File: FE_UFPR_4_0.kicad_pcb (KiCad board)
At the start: 4 copper layers, 146 x 130 mm, 369 parts, among them J1 Mini-Fit Jr 5566-02A, J2 DSUB-37_Socket, J20 LaunchPad J1+J3, J21 LaunchPad J4+J2, J22 LaunchPad J5+J7, J23 LaunchPad J8+J6, J3 LEM DTM13-12PA-R005 key A, J4 ENC DTM13-12PB-R005 key B, J5 VEH DTM13-08PA-R004 key A, Q1 SQD50P06-15L, U1 LMR33630ADDAR, U10 SN74LVC2G17DBVR, U11 SN74LVC2G17DBVR, U12 OPA2376, U13 OPA2376, U14 OPA2376, U15 OPA2376, U16 OPA2376, U17 OPA2376, U18 SN65HVD230DR, U19 LTV-817S-TA1-C, U2 TPS62933FDRLR, U20 LTV-817S-TA1-C, U21 SN74LVC2G17DBVR, U3 AMS1117-3.3, U4 URA2415YMD-6WR3, U5 UCC27524DR, U6 UCC27524DR, U7 UCC27524DR, U8 SN74LVC1G11DBVR, U9 SN74LVC2G17DBVR

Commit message: S9.5: motor temperature channel (EMRAX KTY81-210) on J4 cavities 6/7
The board had no motor-temperature channel at all, and the EMRAX manual
makes one mandatory: the sensor "must be connected to the controller",
120 C on the copper windings voids the warranty, and on sensor
disconnection "the controller has to stop the motor". Captured now
because the board is placed but not yet routed.

Circuit: KTY81-210 as the divider's BOTTOM leg, excited from +3V3 through
R129 2.20k 0.1%. Open -> 3.30 V, short -> 0 V, both outside the valid
1.12-2.18 V band, so disconnect detection is free. +3V3 rather than +5V
so an open sensor cannot exceed the ADC's VDDA+0.3 absolute maximum.
6.25 codes/K at the 120 C limit. R131/R132 monitor the excitation rail on
ADCINA3 so firmware cancels it exactly - without that the LDO's +/-2 % is
+/-10 K, larger than the sensor's own +/-4.7 K.

J4 cavities 6/7 with 5/8 left empty as a guard column; ADC = ADCINB3 on
J20 pad 10. Zero new BOM lines - every part reuses an existing LCSC code.

GATED: legal only if EMRAX confirms the KTY is reinforced-insulated from
the windings. Basic insulation makes it a tractive-system conductor
(FSAE 2026 EV.1.6) and EV.6.5.3 forbids it sharing J4 with the encoder.

Also fixes a PRE-EXISTING defect: sync_schematic_to_board lists nets in
nets_added that it never assigns to pads. +5V_VEH and CAN_RS had ZERO pad
assignments on the board, including in the S9 commit - S10 would have
routed with the ECU supply feed and the CAN slope resistor unconnected.
All twelve pad assignments written directly and confirmed via KiCad's own
IPC-D-356 export.

Gates: netlist re-baselined 220/914 -> 219 nets / 933 nodes (delta fully
accounted); ERC --severity-all 0; DRC --severity-all 0 errors, parity 0.

Co-Authored-By: Claude Opus 5 (1M context) <noreply@anthropic.com>
Claude-Session: https://claude.ai/code/session_016KxKfBKo62GztNqtTupiHA
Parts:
- added C120: 1nF C0G, FE_UFPR_4_0:C_0603_1608Metric, F.Cu at (99.0, 69.5)
- added C121: 22nF C0G, FE_UFPR_4_0:C_0805_2012Metric, F.Cu at (106.0, 92.8)
- added C122: 22nF C0G, FE_UFPR_4_0:C_0805_2012Metric, F.Cu at (102.0, 95.8)
- added D18: BAT54S, FE_UFPR_4_0:SOT-23, F.Cu at (111.0, 92.8)
- added R129: 2.20k 0.1%, FE_UFPR_4_0:R_0603_1608Metric, F.Cu at (94.0, 92.8)
- added R130: 3.3k, FE_UFPR_4_0:R_0603_1608Metric, F.Cu at (102.0, 92.8)
- added R131: 10.0k 0.1%, FE_UFPR_4_0:R_0603_1608Metric, F.Cu at (94.0, 95.8)
- added R132: 10.0k 0.1%, FE_UFPR_4_0:R_0603_1608Metric, F.Cu at (98.0, 95.8)
- added TP53: MOT_TEMP_RAW, FE_UFPR_4_0:TestPoint_Pad_D1.5mm, F.Cu at (98.0, 92.8)
- added TP54: MOT_TEMP_REF, FE_UFPR_4_0:TestPoint_Pad_D1.5mm, F.Cu at (113.5, 97.0)
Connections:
- C119 pad 1: (no net) -> +5V_VEH
- D17 pad 1: (no net) -> +5V_VEH
- F3 pad 1: (no net) -> +5V_VEH
- J20 pad 10: (no net) -> MOT_TEMP_ADC
- J20 pad 12: (no net) -> MOT_TEMP_REF_ADC
- J4 pad 6: (no net) -> MOT_TEMP_RAW
- J4 pad 7: (no net) -> GND
- J5 pad 2: (no net) -> +5V_VEH
- R120 pad 1: (no net) -> CAN_RS
- U18 pad 8: (no net) -> CAN_RS

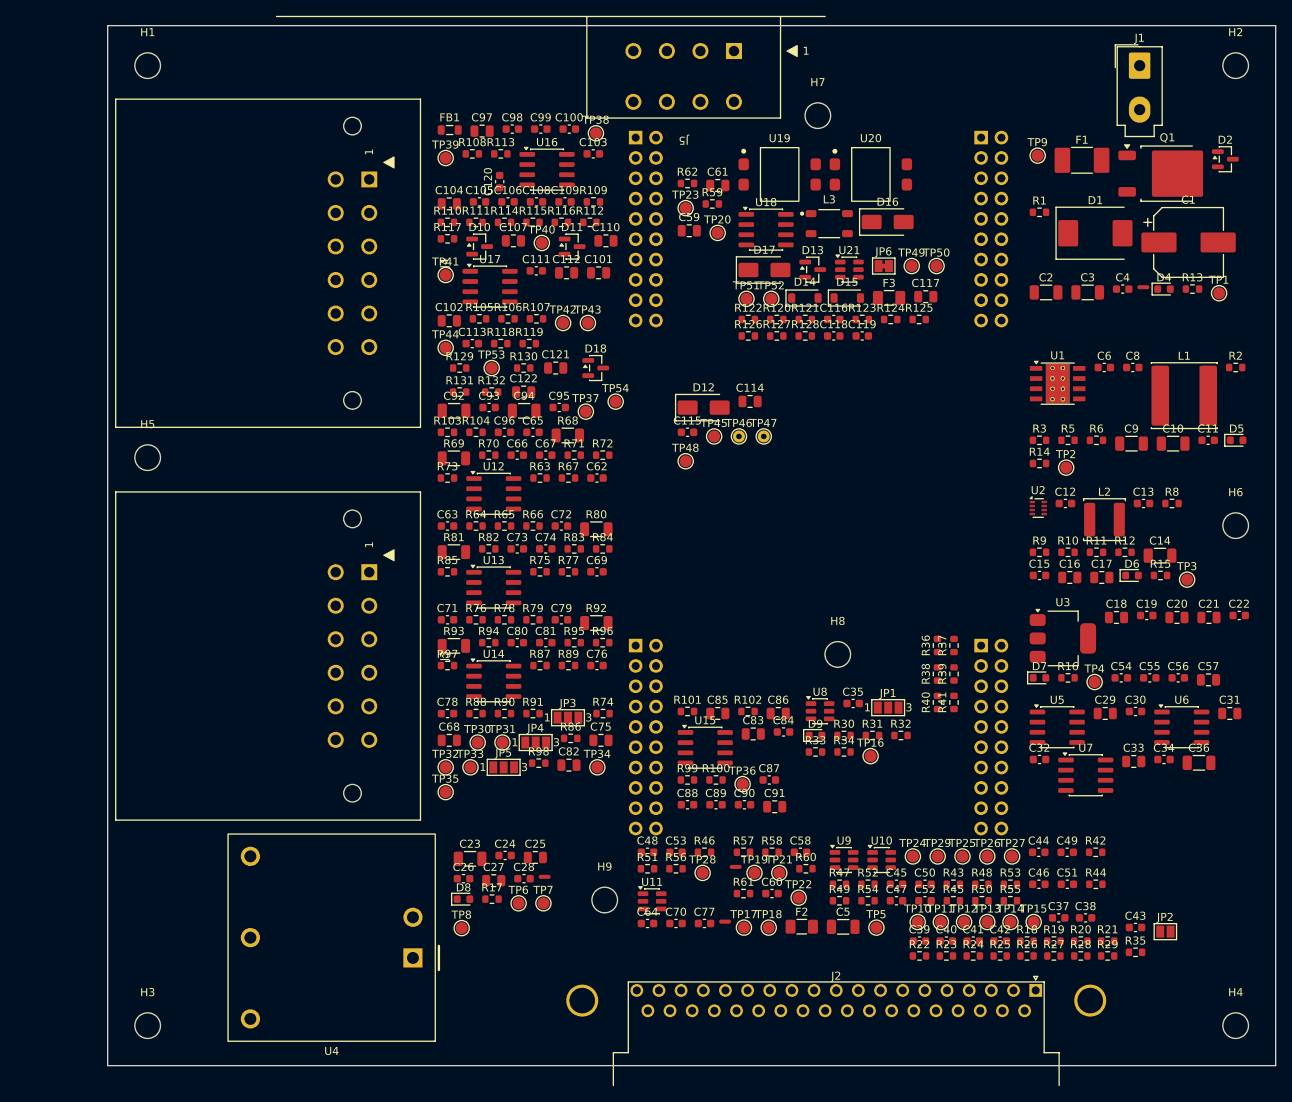
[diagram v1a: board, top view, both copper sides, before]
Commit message: S9.6: vertical mount on X1 via DB37 90° adapter, LaunchPad on top, re-placement (DRC 0 errors)
- Board stands vertical above the PrimeSTACK, DB37 edge down, direct on X1 through an
  L-com DG9037MF right-angle adapter (passive adapter PCB as fallback); the right-angle
  DB37 socket is unchanged so the cable still fits for prototyping.
- All connectors top side: J20-J23 become PinHeader_2x10 on F.Cu (LaunchPad sits above on
  its own receptacles, as on 3.0 - S2's "male pins on top only" premise was wrong). Pad map
  re-verified from KiCad's IPC-D-356 export: 80/80 header pads match golden.net.
- Floorplan re-run: J5 to the top-left clear of the LaunchPad overhang, J4/J3/U4 shifted,
  power column at x >= 120 (LaunchPad shadow drawn on Dwgs.User), new can_end and mot blocks
  (S9.5 parts now in the generator). 370/370 placed, DRC 0 errors, ERC 0.
- golden.net re-baselined: delta is the four header Footprint + LCSC fields only.
- Precharge/DC-bus contactor request documented as PENDING the team (rulebook EV.5.6 /
  EV.7.1.2 conflict) - not drawn.
- Drop two stray LibreOffice lock files from the tree.

Co-Authored-By: Claude Fable 5.1 <noreply@anthropic.com>
Claude-Session: https://claude.ai/code/session_01GDcdscW6XPfxVSLMYKXHdV
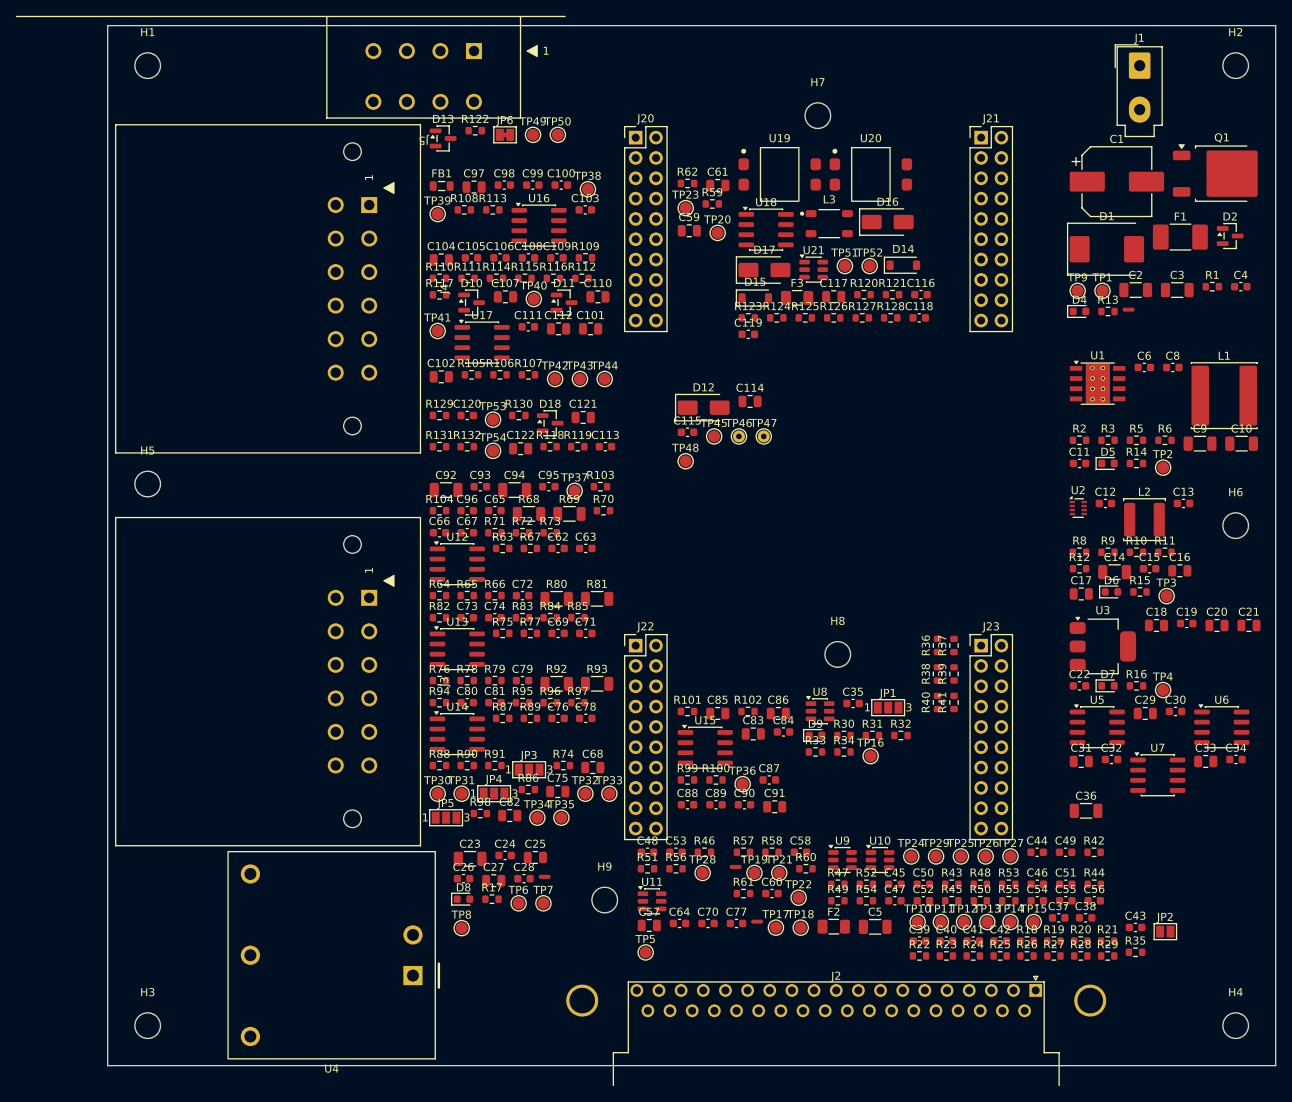
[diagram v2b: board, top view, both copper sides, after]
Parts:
- J20, J21, J22, J23: footprint FE_UFPR_4_0:PinSocket_2x10_P2.54mm_Vertical -> FE_UFPR_4_0:PinHeader_2x10_P2.54mm_Vertical; moved to F.Cu
- moved C57 76.3 mm to (117.7, 162.5)
- moved TP50 50.1 mm to (106.3, 63.6)
- moved JP6 50.1 mm to (99.7, 63.6)
- moved TP49 50.1 mm to (103.2, 63.6)
- moved D13 49.0 mm to (91.9, 64.1)
- moved R122 41.5 mm to (95.9, 63.1)
- moved J5 32.5 mm to (89.5, 56.4)
- moved C54 29.8 mm to (166.2, 159.4)
- moved C55 29.8 mm to (169.8, 159.4)
- moved C56 29.8 mm to (173.3, 159.4)
- moved C120 29.5 mm to (94.9, 98.7), turned to 0 degrees
- moved TP5 29.0 mm to (117.2, 165.8)
- moved R1 23.5 mm to (188.1, 82.6)
- moved C22 21.8 mm to (171.5, 132.5)
- moved R2 21.5 mm to (171.5, 101.8)
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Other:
- board text added: "LAUNCHPAD SHADOW 129.9 x 58.4 - LaunchPad sits ABOVE on J20-J23 (male pins up), ~11 mm stack. Parts under it <= 8 mm tall; test points under it are unreachable when it is fitted."
